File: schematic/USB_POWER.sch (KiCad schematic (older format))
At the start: 4 parts, among them Q1 2N7000, Q2 IRF9540N

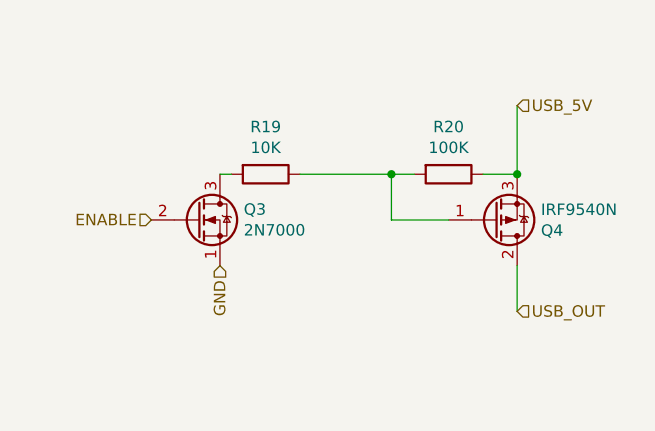
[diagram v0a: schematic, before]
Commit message: Add board, update schematic
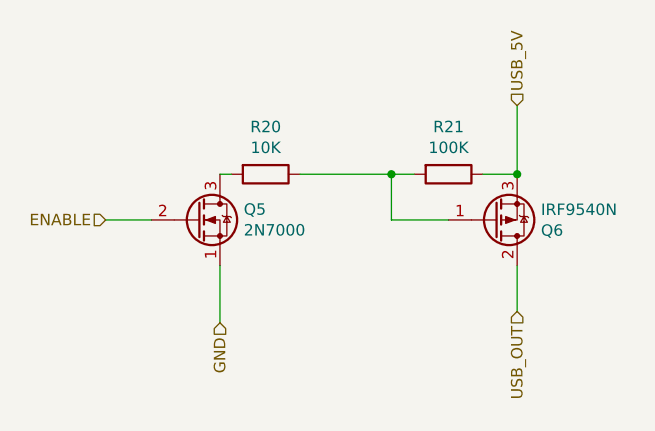
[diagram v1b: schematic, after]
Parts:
- renumbered R17 to R16, R18 to R17
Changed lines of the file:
@@
 $Descr A4 11693 8268
 encoding utf-8
-Sheet 7 8
+Sheet 8 8
 Title ""
 Date ""
@@
 AR Path="/6026DB8E/6025FBC3" Ref="Q4"  Part="1"
 AR Path="/602701A3/6025FBC3" Ref="Q6"  Part="1"
-F 0 "Q4" H 6004 4096 50  0000 L CNN
+F 0 "Q6" H 6004 4096 50  0000 L CNN
 F 1 "IRF9540N" H 6004 4005 50  0000 L CNN
 F 2 "Package_TO_SOT_THT:TO-220-3_Vertical" H 6000 3975 50  0001 L CIN
@@
 P 5600 3850
 AR Path="/60264C97" Ref="R?"  Part="1"
-AR Path="/6025E475/60264C97" Ref="R18"  Part="1"
-AR Path="/6026DB8E/60264C97" Ref="R20"  Part="1"
-AR Path="/602701A3/60264C97" Ref="R22"  Part="1"
-F 0 "R20" V 5393 3850 50  0000 C CNN
+AR Path="/6025E475/60264C97" Ref="R17"  Part="1"
+AR Path="/6026DB8E/60264C97" Ref="R19"  Part="1"
+AR Path="/602701A3/60264C97" Ref="R21"  Part="1"
+F 0 "R21" V 5393 3850 50  0000 C CNN
 F 1 "100K" V 5484 3850 50  0000 C CNN
 F 2 "Resistor_SMD:R_1206_3216Metric" V 5530 3850 50  0001 C CNN
@@
 P 4800 3850
 AR Path="/6026514C" Ref="R?"  Part="1"
-AR Path="/6025E475/6026514C" Ref="R17"  Part="1"
-AR Path="/6026DB8E/6026514C" Ref="R19"  Part="1"
-AR Path="/602701A3/6026514C" Ref="R21"  Part="1"
-F 0 "R19" V 4593 3850 50  0000 C CNN
+AR Path="/6025E475/6026514C" Ref="R16"  Part="1"
+AR Path="/6026DB8E/6026514C" Ref="R18"  Part="1"
+AR Path="/602701A3/6026514C" Ref="R20"  Part="1"
+F 0 "R20" V 4593 3850 50  0000 C CNN
 F 1 "10K" V 4684 3850 50  0000 C CNN
 F 2 "Resistor_SMD:R_1206_3216Metric" V 4730 3850 50  0001 C CNN
@@
 Wire Wire Line
 	5350 4050 5600 4050
-Text HLabel 5900 3550 2    50   Input ~ 0
+Text HLabel 5900 3550 1    50   Input ~ 0
 USB_5V
-Text HLabel 5900 4450 2    50   Input ~ 0
+Text HLabel 5900 4450 3    50   Input ~ 0
 USB_OUT
-Text HLabel 4300 4050 0    50   Input ~ 0
+Text HLabel 4100 4050 0    50   Input ~ 0
 ENABLE
-Text HLabel 4600 4250 3    50   Input ~ 0
+Text HLabel 4600 4500 3    50   Input ~ 0
 GND
 $Comp
@@
 AR Path="/6026DB8E/602613E8" Ref="Q3"  Part="1"
 AR Path="/602701A3/602613E8" Ref="Q5"  Part="1"
-F 0 "Q3" H 4704 4096 50  0000 L CNN
+F 0 "Q5" H 4704 4096 50  0000 L CNN
 F 1 "2N7000" H 4704 4005 50  0000 L CNN
 F 2 "Package_TO_SOT_THT:TO-92_Inline" H 4700 3975 50  0001 L CIN
@@
 Wire Wire Line
 	5900 4450 5900 4250
+Wire Wire Line
+	4600 4250 4600 4500
+Wire Wire Line
+	4300 4050 4100 4050
 $EndSCHEMATC
